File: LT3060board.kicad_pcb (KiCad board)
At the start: 2 copper layers, 7.6 x 24.4 mm, 9 parts, among them IC1 LT3060-TSOT, K1 CONN_3

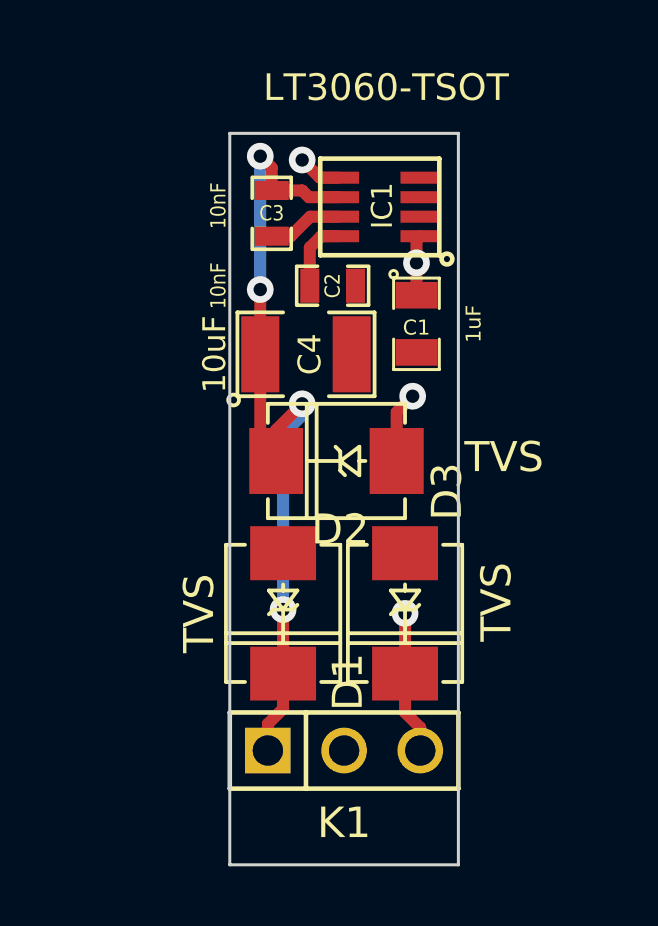
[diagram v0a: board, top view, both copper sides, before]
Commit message: LT3060 protected by more compact TVS-diodes
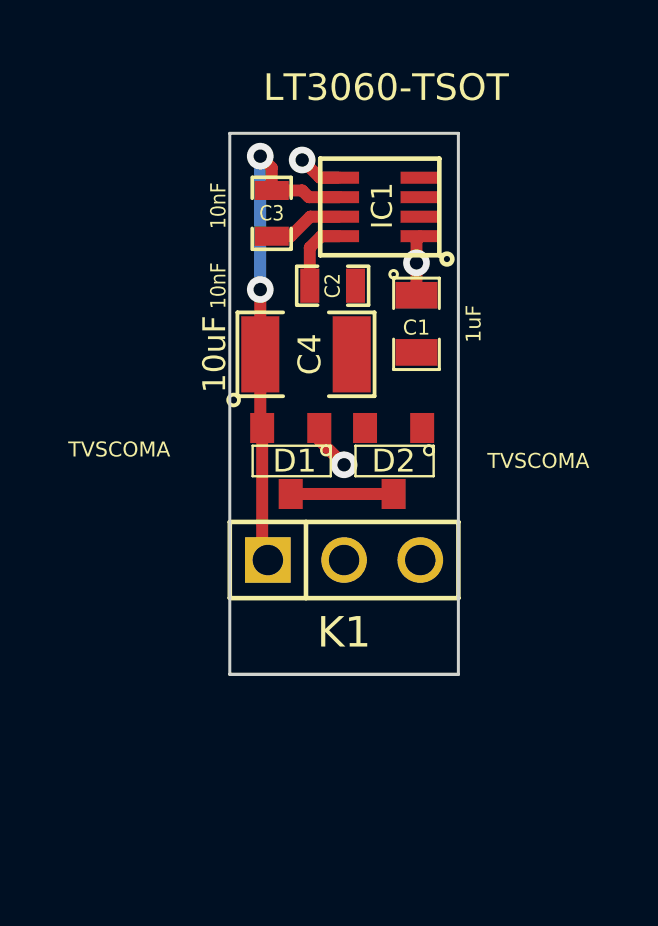
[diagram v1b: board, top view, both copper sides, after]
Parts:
- removed D3: TVS, DO-214AA(SMB)
- D1, D2: value TVS -> TVSCOMA; footprint DO-214AA(SMB) -> SOT23
- moved D1 6.35 mm to (55.4, 60.2), turned to 180 degrees
- moved K1 6.35 mm to (57.1, 63.5)
- moved D2 1.91 mm to (58.8, 60.2)
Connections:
- D1 pad 1: GND -> /Vin
- D1 pad 2: /Vin -> /Vout
- D2 pad 1: /Vin -> GND
- D2 pad 2: /Vout -> GND
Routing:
- net /Vout: track 28.3 -> 17.2 mm, vias 4 -> 2
- net /Vin: track 10.7 -> 5.20 mm, vias 4 -> 3
- net N-000004: track 0.00 -> 3.43 mm
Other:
- board size 7.6 x 24.4 mm -> 7.6 x 18 mm
